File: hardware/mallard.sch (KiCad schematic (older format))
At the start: 0 parts

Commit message: Schematic prepared for Layout
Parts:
- added BatteryPack1: 3.7V, Battery:BatteryHolder_Keystone_1042_1x18650, symbol mallard-rescue:Battery_Cell-Device
- added C1, C10, C12, C13, C14, C2, C3, C4, C5, C6, C7, C8, C9: 1uF, Capacitor_SMD:C_0603_1608Metric_Pad1.08x0.95mm_HandSolder, symbol mallard-rescue:C-Device
- added C11, C15: 10uF, Capacitor_SMD:C_0603_1608Metric_Pad1.08x0.95mm_HandSolder, symbol mallard-rescue:C-Device
- added C16, C17, C18, C19, C20: 0.1uF, Capacitor_SMD:C_0603_1608Metric_Pad1.08x0.95mm_HandSolder, symbol mallard-rescue:C_Small-Device
- added D1: D, Diode_SMD:D_SMA_Handsoldering, symbol mallard-rescue:D-Device
- added D2, D3: LED, LED_SMD:LED_0603_1608Metric_Pad1.05x0.95mm_HandSolder, symbol mallard-rescue:LED-Device
- added D4: Orange, Resistor_SMD:R_0805_2012Metric_Pad1.20x1.40mm_HandSolder, symbol mallard-rescue:LED_Small-Device
- added Eh1, Eh2, Eh3: Eh Electrode, Connector_PinHeader_2.54mm:PinHeader_1x01_P2.54mm_Vertical, symbol mallard-rescue:Conn_01x01-Connector_Generic
- added J1: USB_A, Connector_USB:USB3_A_Molex_48393-001, symbol mallard-rescue:USB_A-Connector
- added J2: Conn_02x03_Odd_Even, Connector_PinHeader_1.27mm:PinHeader_2x03_P1.27mm_Vertical, symbol Connector_Generic:Conn_02x03_Odd_Even
- added J3: Conn_01x03, Connector_PinHeader_2.54mm:PinHeader_1x03_P2.54mm_Vertical_SMD_Pin1Right, symbol Connector_Generic:Conn_01x03
- added R1, R10x1: 5.1k, Resistor_SMD:R_0603_1608Metric_Pad0.98x0.95mm_HandSolder, symbol mallard-rescue:R-Device
- added R10, R19: 20k, Resistor_SMD:R_0201_0603Metric_Pad0.64x0.40mm_HandSolder, symbol mallard-rescue:R-Device
- added R11, R12, R22, R7: Jumper, Resistor_SMD:R_0603_1608Metric_Pad0.98x0.95mm_HandSolder, symbol mallard-rescue:R_Small-Device
- added R13, R17, R4, R6, R8: 10k, Resistor_SMD:R_0201_0603Metric_Pad0.64x0.40mm_HandSolder, symbol mallard-rescue:R-Device
- added R14: 1k, Resistor_SMD:R_0201_0603Metric_Pad0.64x0.40mm_HandSolder, symbol mallard-rescue:R-Device
- added R15: 30k, Resistor_SMD:R_0201_0603Metric_Pad0.64x0.40mm_HandSolder, symbol mallard-rescue:R-Device
- added R16: 20k DNI, Resistor_SMD:R_0201_0603Metric_Pad0.64x0.40mm_HandSolder, symbol mallard-rescue:R-Device
- added R18: 9.1k, Resistor_SMD:R_0201_0603Metric_Pad0.64x0.40mm_HandSolder, symbol mallard-rescue:R-Device
- added R2: 21.5k, Resistor_SMD:R_0603_1608Metric_Pad0.98x0.95mm_HandSolder, symbol mallard-rescue:R-Device
- added R20: 80.6k, Resistor_SMD:R_0603_1608Metric_Pad0.98x0.95mm_HandSolder, symbol mallard-rescue:R-Device
- added R21: 324k, Resistor_SMD:R_0603_1608Metric_Pad0.98x0.95mm_HandSolder, symbol mallard-rescue:R-Device
- added R23: 680, Resistor_SMD:R_0603_1608Metric_Pad0.98x0.95mm_HandSolder, symbol mallard-rescue:R_Small-Device
- added R24: 10k, Resistor_SMD:R_0201_0603Metric_Pad0.64x0.40mm_HandSolder, symbol mallard-rescue:R_Small-Device
- added R3, R5: 3.6k, Resistor_SMD:R_0603_1608Metric_Pad0.98x0.95mm_HandSolder, symbol mallard-rescue:R-Device
- added R9: Jumper DNI, Resistor_SMD:R_0603_1608Metric_Pad0.98x0.95mm_HandSolder, symbol mallard-rescue:R_Small-Device
- added Ref1: Conn_01x02, Connector_Coaxial:BNC_TEConnectivity_1478204_Vertical, symbol Connector_Generic:Conn_01x02
- added SM1, SM2, SM3: Conn_01x03, Connector_PinHeader_2.54mm:PinHeader_1x03_P2.54mm_Vertical_SMD_Pin1Right, symbol mallard-rescue:Conn_01x03-Connector_Generic
- added SW1: RESET Switch, Button_Switch_SMD:SW_SPST_B3U-1000P, symbol Switch:SW_Push
- added TH1: 103AT, Resistor_THT:R_Axial_DIN0204_L3.6mm_D1.6mm_P2.54mm_Vertical, symbol mallard-rescue:Thermistor-Device
- added U1, U2, U3: TMP235, Connector_PinHeader_2.54mm:PinHeader_1x05_P2.54mm_Vertical, symbol mallard:TMP235
- added U10: LTC1983ES6-3, Package_TO_SOT_SMD:SOT-23-6, symbol mallard:LTC1983ES6-3
- added U11: STM32L4Q5xx, Package_QFP:LQFP-48_7x7mm_P0.5mm, symbol mallard-rescue:STM32L431CBTx-MCU_ST_STM32L4
- added U4: BQ24210DQCT, Package_SON:WSON-10-1EP_2x3mm_P0.5mm_EP0.84x2.4mm, symbol mallard:BQ24210DQCT
- added U5, U6: TMUX1309, Package_DFN_QFN:WQFN-16-1EP_3x3mm_P0.5mm_EP1.6x1.6mm, symbol mallard:TMUX1309
- added U7: LMP7721, Package_SO:SOIC-8_3.9x4.9mm_P1.27mm, symbol mallard:LMP7721
- added U8: TPS71710DRVR, Package_SON:WSON-6-1EP_2x2mm_P0.65mm_EP1x1.6mm, symbol mallard:TPS717
- added U9: LMV554, Package_SO:TSSOP-14_4.4x5mm_P0.65mm, symbol mallard:LMV554
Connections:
- new net: D4.1 (K), U11.40 (PB4)
- new net: D4.2 (A), R23.2
- new net: Eh1.1 (Pin_1), U5.1 (S0B)
- new net: Eh2.1 (Pin_1), U5.5 (S1B)
- new net: Eh3.1 (Pin_1), U5.2 (S2B)
- new net: SM1.2 (Pin_2), U5.12 (S0A)
- new net: SM2.2 (Pin_2), U5.14 (S1A)
- new net: SM3.2 (Pin_2), U5.15 (S2A)
- new net: R4.2, U5.3 (DB)
- new net: R4.1, R6.1, R7.2, R9.2
- new net: R16.1, R17.1, U9.1 (OUT_A)
- new net: R10.1, R15.2, R16.2, U9.6 (IN_B-)
- new net: U6.13 (DA), U9.10 (IN_C+)
- new net: R11.1, R12.1, U9.12 (IN_D+)
- new net: R14.1, R18.2, U9.13 (IN_D-)
- new net: R17.2, R9.1, U9.2 (IN_A-)
- new net: R13.2, R19.2, U9.9 (IN_C-)
- new net: U1.3 (Vout), U6.12 (S0A)
- new net: U2.3 (Vout), U6.14 (S1A)
- new net: U3.3 (Vout), U6.15 (S2A)
- new net: R11.2, Ref1.1 (Pin_1)
- new net: R12.2, Ref1.2 (Pin_2)
- new net: R10.2, R8.1, U7.4 (Vout)
- new net: R7.1, R8.2, U7.8 (IN-)
- new net: D3.1 (K), U4.6 (PG)
- new net: D3.2 (A), R5.2
- new net: R2.1, U4.4 (VTSB)
- new net: R2.2, TH1.2, U4.5 (TS)
- new net: D2.2 (A), R3.2
- new net: C13.1, U10.3 (C+)
- new net: C13.2, U10.4 (C-)
- new net: R1.1, U4.2 (ISET)
- new net: C4.1, D1.1 (K), U4.1 (VBUS)
- new net: D2.1 (K), U4.8 (CHG)
- new net: R10x1.1, U4.9 (VDPM)
- new net: C14.1, R20.1, R22.2, U8.1 (OUT)
- new net: R20.2, R21.1, U8.2 (FB)
- new net +1V0: R22.1, R6.2
- new net +1V0_EN: U11.25 (PB12), U8.4 (EN)
- new net +3V3: BatteryPack1.1 (+), C1.1, C10.1, C11.1, C12.1, C16.1, C17.1, C18.1, C19.1, C2.1, C20.1, C3.1, C5.1, C6.1, C7.1, C8.1, J2.5 (Pin_5), R23.1, R24.2, R3.1, R5.1, SM1.1 (Pin_1), SM2.1 (Pin_1), SM3.1 (Pin_1), U1.4 (VCC), U10.1 (Vin), U11.1 (VBAT), U11.24 (VDD), U11.36 (VDDUSB), U11.48 (VDD), U11.9 (VDDA), U2.4 (VCC), U3.4 (VCC), U4.10 (BAT), U5.16 (VDD), U6.16 (VDD), U7.6 (V+), U8.6 (IN), U9.4 (V+)
- new net +5V: J1.1 (VBUS)
- new net -3V3: C15.1, C9.1, U10.2 (Vout), U7.3 (V-), U9.11 (V-)
- new net -3V3_SHDN_L: U10.6 (SHDN)
- new net CP_SHDN_L: U11.22 (PB11)
- new net Charge_EN: U11.21 (PB10), U4.7 (EN)
- new net Eh_Sense: R15.1, U11.10 (PA0), U9.7 (OUT_B)
- new net GND: BatteryPack1.2 (-), C1.2, C10.2, C11.2, C12.2, C14.2, C15.2, C16.2, C17.2, C18.2, C19.2, C2.2, C20.2, C3.2, C4.2, C5.2, C6.2, C7.2, C8.2, C9.2, J1.4 (GND), J1.5 (Shield), J2.2 (Pin_2), J3.3 (Pin_3), R1.2, R10x1.2, R13.1, R14.2, R21.2, SM1.3 (Pin_3), SM2.3 (Pin_3), SM3.3 (Pin_3), SW1.1, TH1.1, U1.2 (GND), U10.5 (GND), U11.23 (VSS), U11.35 (VSS), U11.47 (VSS), U11.8 (VSSA), U2.2 (GND), U3.2 (GND), U4.3 (VSS), U5.8 (GND), U6.8 (GND), U7.1 (IN+), U8.3 (GND), U8.7 (GND), U9.3 (IN_A+), U9.5 (IN_B+)
- new net MUX1_A0: U11.15 (PA5), U5.9 (A1)
- new net MUX1_A1: U11.16 (PA6), U5.10 (A0)
- new net MUX1_EN: U11.14 (PA4), U5.6 (EN)
- new net MUX2_A0: U11.19 (PB1), U6.9 (A1)
- new net MUX2_A1: U11.20 (PB2), U6.10 (A0)
- new net MUX2_EN: U11.18 (PB0), U6.6 (EN)
- new net Moisture_Sense: U11.13 (PA3), U5.13 (DA)
- new net RESET_L: J2.6 (Pin_6), R24.1, SW1.2, U11.7 (NRST)
- new net Ref_Elec: U11.12 (PA2)
- new net Ref_Out: R18.1, U9.14 (OUT_D)
- new net SWCLK: J2.3 (Pin_3), U11.37 (PA14)
- new net SWDIO: J2.1 (Pin_1), U11.34 (PA13)
- new net Temp_Sense: R19.1, U11.11 (PA1), U9.8 (OUT_C)
- new net USART1_RX: J3.2 (Pin_2), U11.31 (PA10)
- new net USART1_TX: J3.1 (Pin_1), U11.30 (PA9)
- new net USB+: J1.3 (D+), U11.32 (PA11)
- new net USB-: J1.2 (D-), U11.33 (PA12)
- no-connect marks 0 -> 3
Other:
- note added: "Check Symbol with Datasheet to make sure pins match"
- note added: "DNI VDPM Resistor"
- note added: "Double check footprint for USB connector"
- note added: "FOOTPRINT FOR TMP235 IS 5 HOLE CONNECTOR"
- note added: "I have these switches on hand"
- note added: "May have to find alt thermistor...\nNeed B=3435K"
- note added: "Programming connector copied from a previous project (Flamingo)"
- note added: "SOLAR_PANEL"
- note added: "Soil Moisture Output"

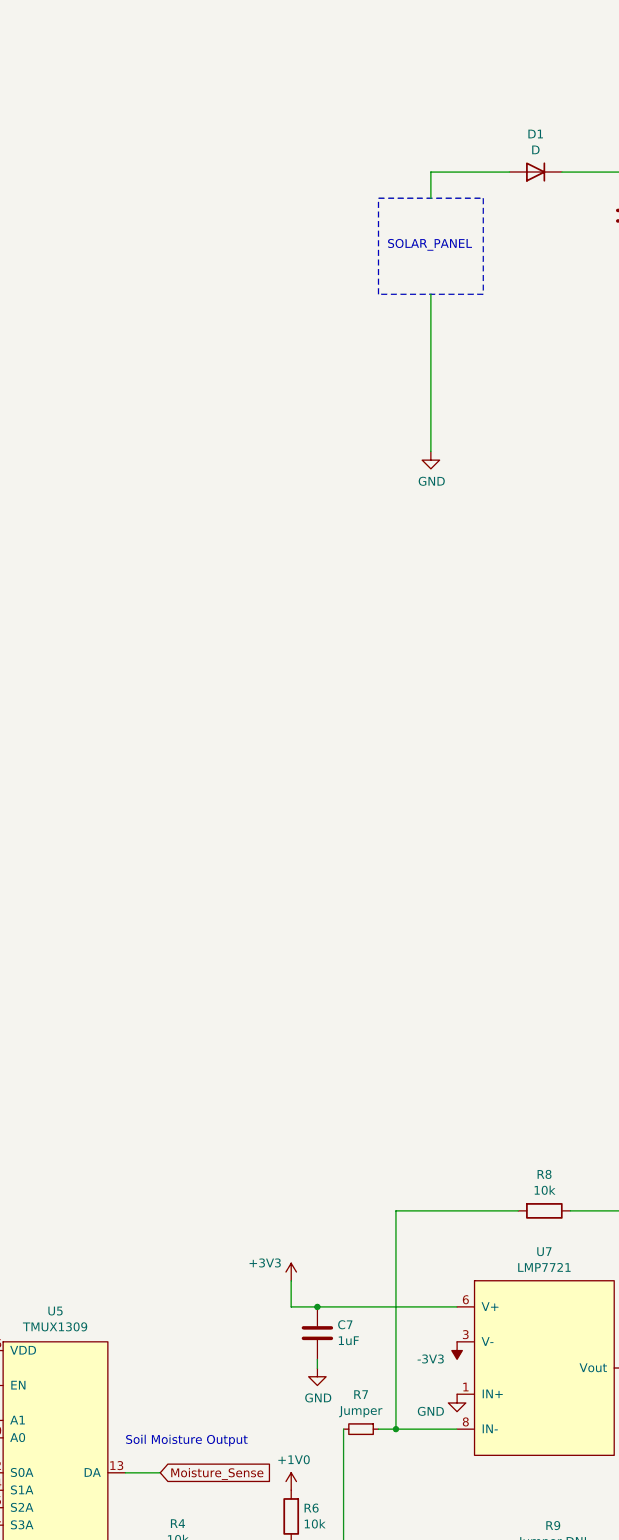
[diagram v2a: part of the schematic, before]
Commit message: Added screw terminals for solar panel, and added a cap
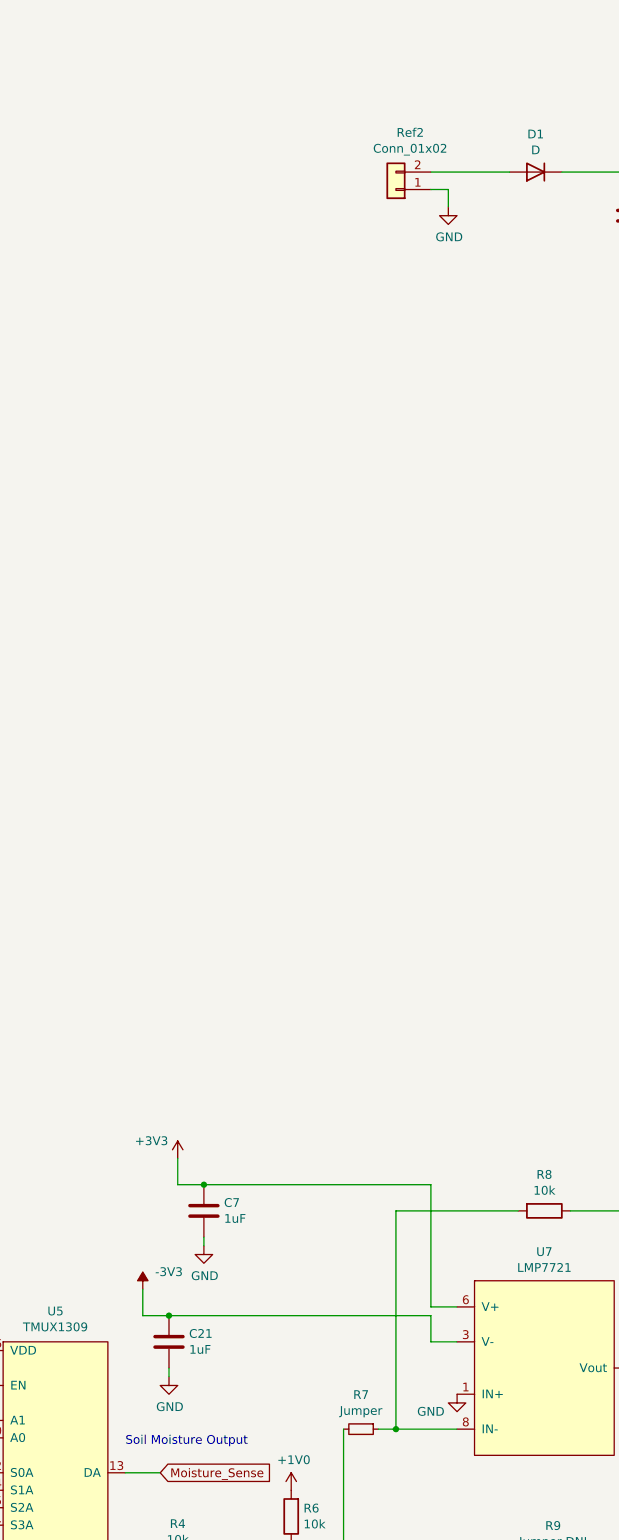
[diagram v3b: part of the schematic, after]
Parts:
- added C21: 1uF, Capacitor_SMD:C_0603_1608Metric_Pad1.08x0.95mm_HandSolder, symbol mallard-rescue:C-Device
- added Ref2: Conn_01x02, mallard:mallardScrewTerm., symbol Connector_Generic:Conn_01x02
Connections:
- net -3V3: now also C21.1
- net GND: now also C21.2, Ref2.1 (Pin_1)
- net at D1.2 (A): now also Ref2.2 (Pin_2)
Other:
- note removed: "SOLAR_PANEL"
- moved on the sheet: C7
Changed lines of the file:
@@
 L mallard-rescue:-3V3-power #PWR?
 U 1 1 61FEBA5C
-P 1150 9700
+P -650 9400
 AR Path="/60B3FE92/61FEBA5C" Ref="#PWR?"  Part="1"
 AR Path="/61FEBA5C" Ref="#PWR0140"  Part="1"
-F 0 "#PWR0140" H 1150 9800 50  0001 C CNN
-F 1 "-3V3" H 1000 9800 50  0000 C CNN
-F 2 "" H 1150 9700 50  0001 C CNN
-F 3 "" H 1150 9700 50  0001 C CNN
-	1    1150 9700
-	1    0    0    1
+F 0 "#PWR0140" H -650 9500 50  0001 C CNN
+F 1 "-3V3" H -800 9500 50  0000 C CNN
+F 2 "" H -650 9400 50  0001 C CNN
+F 3 "" H -650 9400 50  0001 C CNN
+	1    -650 9400
+	-1   0    0    -1
 $EndComp
 $Comp
 L mallard-rescue:+3V3-power #PWR?
 U 1 1 61FEBA62
-P 200 9350
+P -450 8650
 AR Path="/60B3FE92/61FEBA62" Ref="#PWR?"  Part="1"
 AR Path="/61FEBA62" Ref="#PWR0141"  Part="1"
-F 0 "#PWR0141" H 200 9200 50  0001 C CNN
-F 1 "+3V3" H 50  9450 50  0000 C CNN
-F 2 "" H 200 9350 50  0001 C CNN
-F 3 "" H 200 9350 50  0001 C CNN
-	1    200  9350
+F 0 "#PWR0141" H -450 8500 50  0001 C CNN
+F 1 "+3V3" H -600 8750 50  0000 C CNN
+F 2 "" H -450 8650 50  0001 C CNN
+F 3 "" H -450 8650 50  0001 C CNN
+	1    -450 8650
 	1    0    0    -1
 $EndComp
@@
 L mallard-rescue:GND-power #PWR?
 U 1 1 61FEBA9C
-P 350 9850
+P -300 9150
 AR Path="/60B3FF2D/61FEBA9C" Ref="#PWR?"  Part="1"
 AR Path="/60B3FE92/61FEBA9C" Ref="#PWR?"  Part="1"
 AR Path="/61FEBA9C" Ref="#PWR0143"  Part="1"
-F 0 "#PWR0143" H 350 9600 50  0001 C CNN
-F 1 "GND" H 355 9677 50  0000 C CNN
-F 2 "" H 350 9850 50  0001 C CNN
-F 3 "" H 350 9850 50  0001 C CNN
-	1    350  9850
+F 0 "#PWR0143" H -300 8900 50  0001 C CNN
+F 1 "GND" H -295 8977 50  0000 C CNN
+F 2 "" H -300 9150 50  0001 C CNN
+F 3 "" H -300 9150 50  0001 C CNN
+	1    -300 9150
 	1    0    0    -1
 $EndComp
@@
 L mallard-rescue:C-Device C?
 U 1 1 61FEBAA3
-P 350 9650
+P -300 8950
 AR Path="/60B3FF2D/61FEBAA3" Ref="C?"  Part="1"
 AR Path="/60B3FE92/61FEBAA3" Ref="C?"  Part="1"
 AR Path="/61FEBAA3" Ref="C7"  Part="1"
-F 0 "C7" H 465 9696 50  0000 L CNN
-F 1 "1uF" H 465 9605 50  0000 L CNN
-F 2 "Capacitor_SMD:C_0603_1608Metric_Pad1.08x0.95mm_HandSolder" H 388 9500 50  0001 C CNN
-F 3 "https://www.yageo.com/upload/media/product/productsearch/datasheet/mlcc/UPY-GPHC_X7R_6.3V-to-50V_20.pdf" H 350 9650 50  0001 C CNN
-F 4 "311-1446-1-ND" H 350 9650 50  0001 C CNN "Digikey"
-	1    350  9650
-	1    0    0    -1
-$EndComp
-Wire Wire Line
-	350  9800 350  9850
-Wire Wire Line
-	200  9350 200  9500
-Wire Wire Line
-	200  9500 350  9500
-Wire Wire Line
-	350  9500 1150 9500
-Connection ~ 350  9500
+F 0 "C7" H -185 8996 50  0000 L CNN
+F 1 "1uF" H -185 8905 50  0000 L CNN
+F 2 "Capacitor_SMD:C_0603_1608Metric_Pad1.08x0.95mm_HandSolder" H -262 8800 50  0001 C CNN
+F 3 "https://www.yageo.com/upload/media/product/productsearch/datasheet/mlcc/UPY-GPHC_X7R_6.3V-to-50V_20.pdf" H -300 8950 50  0001 C CNN
+F 4 "311-1446-1-ND" H -300 8950 50  0001 C CNN "Digikey"
+	1    -300 8950
+	1    0    0    -1
+$EndComp
+Wire Wire Line
+	-300 9100 -300 9150
+Wire Wire Line
+	-450 8650 -450 8800
+Wire Wire Line
+	-450 8800 -300 8800
+Connection ~ -300 8800
 $Comp
 L mallard-rescue:GND-power #PWR?
@@
 	1    0    0    -1
 $EndComp
-Wire Notes Line
-	1300 3150 1300 3700
-Wire Notes Line
-	1300 3700 700  3700
-Wire Notes Line
-	700  3700 700  3150
-Wire Notes Line
-	700  3150 1300 3150
-Text Notes 750  3450 0    50   ~ 0
-SOLAR_PANEL
 $Comp
 L mallard-rescue:GND-power #PWR0152
 U 1 1 620370A7
-P 1000 4600
-F 0 "#PWR0152" H 1000 4350 50  0001 C CNN
-F 1 "GND" H 1005 4427 50  0000 C CNN
-F 2 "" H 1000 4600 50  0001 C CNN
-F 3 "" H 1000 4600 50  0001 C CNN
-	1    1000 4600
+P 1100 3200
+F 0 "#PWR0152" H 1100 2950 50  0001 C CNN
+F 1 "GND" H 1105 3027 50  0000 C CNN
+F 2 "" H 1100 3200 50  0001 C CNN
+F 3 "" H 1100 3200 50  0001 C CNN
+	1    1100 3200
 	1    0    0    -1
 $EndComp
@@
 Wire Wire Line
 	2150 3400 2150 3650
-Wire Wire Line
-	1000 3000 1000 3150
 Wire Wire Line
 	6950 3000 7350 3000
@@
 Wire Wire Line
 	6950 3000 6950 3600
-Wire Wire Line
-	1000 3700 1000 4600
 Wire Wire Line
 	5300 3000 6200 3000
@@
 Text Notes 12650 750  0    50   ~ 0
 Programming connector copied from a previous project (Flamingo)
+$Comp
+L Connector_Generic:Conn_01x02 Ref?
+U 1 1 61F0B90F
+P 800 3100
+AR Path="/60B3FE92/61F0B90F" Ref="Ref?"  Part="1"
+AR Path="/61F0B90F" Ref="Ref2"  Part="1"
+F 0 "Ref2" H 718 2775 50  0000 C CNN
+F 1 "Conn_01x02" H 718 2866 50  0000 C CNN
+F 2 "mallard:mallardScrewTerm." H 800 3100 50  0001 C CNN
+F 3 "" H 800 3100 50  0001 C CNN
+F 4 "" H 800 3100 50  0001 C CNN "Digikey"
+	1    800  3100
+	-1   0    0    1
+$EndComp
+Wire Wire Line
+	1000 3100 1100 3100
+Wire Wire Line
+	1100 3100 1100 3200
+$Comp
+L mallard-rescue:GND-power #PWR?
+U 1 1 61F6F90F
+P -500 9900
+AR Path="/60B3FF2D/61F6F90F" Ref="#PWR?"  Part="1"
+AR Path="/60B3FE92/61F6F90F" Ref="#PWR?"  Part="1"
+AR Path="/61F6F90F" Ref="#PWR0168"  Part="1"
+F 0 "#PWR0168" H -500 9650 50  0001 C CNN
+F 1 "GND" H -495 9727 50  0000 C CNN
+F 2 "" H -500 9900 50  0001 C CNN
+F 3 "" H -500 9900 50  0001 C CNN
+	1    -500 9900
+	1    0    0    -1
+$EndComp
+$Comp
+L mallard-rescue:C-Device C?
+U 1 1 61F6F916
+P -500 9700
+AR Path="/60B3FF2D/61F6F916" Ref="C?"  Part="1"
+AR Path="/60B3FE92/61F6F916" Ref="C?"  Part="1"
+AR Path="/61F6F916" Ref="C21"  Part="1"
+F 0 "C21" H -385 9746 50  0000 L CNN
+F 1 "1uF" H -385 9655 50  0000 L CNN
+F 2 "Capacitor_SMD:C_0603_1608Metric_Pad1.08x0.95mm_HandSolder" H -462 9550 50  0001 C CNN
+F 3 "https://www.yageo.com/upload/media/product/productsearch/datasheet/mlcc/UPY-GPHC_X7R_6.3V-to-50V_20.pdf" H -500 9700 50  0001 C CNN
+F 4 "311-1446-1-ND" H -500 9700 50  0001 C CNN "Digikey"
+	1    -500 9700
+	1    0    0    -1
+$EndComp
+Wire Wire Line
+	-500 9850 -500 9900
+Wire Wire Line
+	-650 9400 -650 9550
+Wire Wire Line
+	-650 9550 -500 9550
+Connection ~ -500 9550
+Wire Wire Line
+	1000 8800 1000 9500
+Wire Wire Line
+	1000 9500 1150 9500
+Wire Wire Line
+	-300 8800 1000 8800
+Wire Wire Line
+	1000 9550 1000 9700
+Wire Wire Line
+	1000 9700 1150 9700
+Wire Wire Line
+	-500 9550 1000 9550
 $EndSCHEMATC

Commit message: Schematic finished, layout stared
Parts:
- removed C2, C3: 1uF, Capacitor_SMD:C_0603_1608Metric_Pad1.08x0.95mm_HandSolder, symbol mallard-rescue:C-Device
- added C? (x2): 1uF, Capacitor_SMD:C_0603_1608Metric_Pad1.08x0.95mm_HandSolder, symbol mallard-rescue:C-Device
- added C?: 3.3uF, symbol Device:C_Small
- added C?: 10uF, symbol Device:C_Small
- added D?: RED, symbol Device:D_Small
- added J? (x3): Conn_01x03, symbol Connector_Generic:Conn_01x03
- added L?: 4.7uH, symbol Device:L
- added R?: 370, symbol Device:R_Small
- added U?: LTC3529EDCB, symbol mallard:LTC3529EDCB
- U1, U2, U3: footprint Connector_PinHeader_2.54mm:PinHeader_1x05_P2.54mm_Vertical -> (none)
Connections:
- net +3V3: now also C?.1, C?.1, C?.1, D?.2 (A), J?.1 (Pin_1), J?.1 (Pin_1), J?.1 (Pin_1), L?.1, U?.8 (Vin); no longer U1.4 (VCC), U2.4 (VCC), U3.4 (VCC)
- net +5V: now also C?.1, U?.1 (Vout)
- net -3V3_SHDN_L: now also U11.28 (PB15)
- net GND: now also C?.2, C?.2, C?.2, C?.2, J?.3 (Pin_3), J?.3 (Pin_3), J?.3 (Pin_3), U?.4 (PGND), U?.6 (SNSGND); no longer U1.2 (GND), U2.2 (GND), U3.2 (GND)
- net 5V_RST: now reaches U11.26 (PB13)
- net 5V_RST: now also U?.7 (RST)
- net 5V_SHDN_L: now reaches U11.27 (PB14)
- net 5V_SHDN_L: now also U?.3 (SHDN)
- net at U6.12 (S0A): now also J?.2 (Pin_2); no longer U1.3 (Vout)
- net at U6.14 (S1A): now also J?.2 (Pin_2); no longer U2.3 (Vout)
- net at U6.15 (S2A): now also J?.2 (Pin_2); no longer U3.3 (Vout)
- new net: L?.2, U?.2 (SW)
- new net: R?.1, U?.5 (FAULT)
- new net: D?.1 (K), R?.2
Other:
- note added: "Wrong footprint size"
- moved on the sheet: C1, C10, C21, C5, C6, C7, C9, Eh1, Eh2, Eh3, R10, R11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

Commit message: Modified footprints and added items to BOM
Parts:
- C? (x2): footprint (none) -> Capacitor_SMD:C_0603_1608Metric_Pad1.08x0.95mm_HandSolder
- D?: footprint (none) -> LED_SMD:LED_0603_1608Metric_Pad1.05x0.95mm_HandSolder
- J? (x3): footprint (none) -> Connector_PinHeader_2.54mm:PinHeader_1x03_P2.54mm_Vertical
- L?: footprint (none) -> Inductor_SMD:L_0805_2012Metric_Pad1.05x1.20mm_HandSolder
- R?: footprint (none) -> Resistor_SMD:R_0603_1608Metric_Pad0.98x0.95mm_HandSolder
- U?: footprint (none) -> mallard:DFN200X300X80-9N
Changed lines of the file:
@@
 F 0 "J?" H -4032 12175 50  0000 C CNN
 F 1 "Conn_01x03" H -4032 12266 50  0000 C CNN
-F 2 "" H -3950 12500 50  0001 C CNN
+F 2 "Connector_PinHeader_2.54mm:PinHeader_1x03_P2.54mm_Vertical" H -3950 12500 50  0001 C CNN
 F 3 "~" H -3950 12500 50  0001 C CNN
 	1    -3950 12500
@@
 F 0 "J?" H -3782 13175 50  0000 C CNN
 F 1 "Conn_01x03" H -3782 13266 50  0000 C CNN
-F 2 "" H -3700 13500 50  0001 C CNN
+F 2 "Connector_PinHeader_2.54mm:PinHeader_1x03_P2.54mm_Vertical" H -3700 13500 50  0001 C CNN
 F 3 "~" H -3700 13500 50  0001 C CNN
 	1    -3700 13500
@@
 F 0 "J?" H -3782 14175 50  0000 C CNN
 F 1 "Conn_01x03" H -3782 14266 50  0000 C CNN
-F 2 "" H -3700 14500 50  0001 C CNN
+F 2 "Connector_PinHeader_2.54mm:PinHeader_1x03_P2.54mm_Vertical" H -3700 14500 50  0001 C CNN
 F 3 "~" H -3700 14500 50  0001 C CNN
 	1    -3700 14500
@@
 F 0 "U?" H 2750 6125 50  0000 C CNN
 F 1 "LTC3529EDCB" H 2750 6034 50  0000 C CNN
-F 2 "" H 2300 6100 50  0001 C CNN
+F 2 "mallard:DFN200X300X80-9N" H 2300 6100 50  0001 C CNN
 F 3 "https://www.analog.com/media/en/technical-documentation/data-sheets/3529fb.pdf" H 2300 6100 50  0001 C CNN
 F 4 "LTC3529EDCB#TRPBF" H 2400 5950 50  0001 C CNN "Digikey"
@@
 F 0 "C?" H 1550 5900 50  0000 L CNN
 F 1 "3.3uF" H 1450 5800 50  0000 L CNN
-F 2 "" H 1750 5850 50  0001 C CNN
+F 2 "Capacitor_SMD:C_0603_1608Metric_Pad1.08x0.95mm_HandSolder" H 1750 5850 50  0001 C CNN
 F 3 "~" H 1750 5850 50  0001 C CNN
 	1    1750 5850
@@
 F 0 "R?" V 1950 6200 50  0000 C CNN
 F 1 "370" V 2050 6200 50  0000 C CNN
-F 2 "" H 2150 6200 50  0001 C CNN
+F 2 "Resistor_SMD:R_0603_1608Metric_Pad0.98x0.95mm_HandSolder" H 2150 6200 50  0001 C CNN
 F 3 "~" H 2150 6200 50  0001 C CNN
 	1    2150 6200
@@
 F 0 "C?" H 3692 6446 50  0000 L CNN
 F 1 "10uF" H 3692 6355 50  0000 L CNN
-F 2 "" H 3600 6400 50  0001 C CNN
+F 2 "Capacitor_SMD:C_0603_1608Metric_Pad1.08x0.95mm_HandSolder" H 3600 6400 50  0001 C CNN
 F 3 "~" H 3600 6400 50  0001 C CNN
 	1    3600 6400
@@
 F 0 "L?" V 2940 5650 50  0000 C CNN
 F 1 "4.7uH" V 2849 5650 50  0000 C CNN
-F 2 "" H 2750 5650 50  0001 C CNN
+F 2 "Inductor_SMD:L_0805_2012Metric_Pad1.05x1.20mm_HandSolder" H 2750 5650 50  0001 C CNN
 F 3 "~" H 2750 5650 50  0001 C CNN
 F 4 "ASMCI-0805-4R7M-T" V 2750 5650 50  0001 C CNN "Digikey"
@@
 F 0 "D?" V 1996 5782 50  0000 R CNN
 F 1 "RED" V 1905 5782 50  0000 R CNN
-F 2 "" V 1950 5850 50  0001 C CNN
+F 2 "LED_SMD:LED_0603_1608Metric_Pad1.05x0.95mm_HandSolder" V 1950 5850 50  0001 C CNN
 F 3 "~" V 1950 5850 50  0001 C CNN
 	1    1950 5850
